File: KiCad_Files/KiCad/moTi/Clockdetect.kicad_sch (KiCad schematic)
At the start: 12 parts, among them Q1 NTK3139PT5G, U2 TLV3511DCKR, U5 SN74LVC1G3157DRLR

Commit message: HW file update
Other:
- title: MosaicTimeSync -> moTi
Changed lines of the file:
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@@
 	(paper "A3")
 	(title_block
-		(title "MosaicTimeSync")
+		(title "moTi")
 		(date "2025-09-02")
 		(rev "01")
@@
 		(comment 2 "Programme under the Fundamental Elements ")
 		(comment 3 "co-funded by the European Union Agency for the Space ")
-		(comment 4 "MosaicTimeSync project has been documented by Septentrio")
+		(comment 4 "moTi project has been documented by Septentrio")
 	)
 	(rectangle
@@
 				)
 				(justify right)
+				(hide yes)
 			)
 		)
@@
 				)
 				(justify left)
+				(hide yes)
 			)
 		)
@@
 				)
 				(justify left)
+				(hide yes)
 			)
 		)
@@
 				)
 				(justify left)
+				(hide yes)
 			)
 		)
@@
 				)
 				(justify right)
+				(hide yes)
 			)
 		)
@@
 				)
 				(justify right)
+				(hide yes)
 			)
 		)
@@
 		(dnp no)
 		(fields_autoplaced yes)
-		(property "Reference" "#PWR038"
+		(property "Reference" "#PWR?"
 			(at 114.3 45.72 0)
 			(effects
@@
 		(on_board yes)
 		(dnp no)
-		(property "Reference" "U2"
+		(property "Reference" "U?"
 			(at 298.196 174.244 0)
 			(effects
@@
 		(on_board yes)
 		(dnp no)
-		(property "Reference" "R11"
+		(property "Reference" "R?"
 			(at 267.97 180.848 90)
 			(effects
@@
 		(dnp no)
 		(fields_autoplaced yes)
-		(property "Reference" "C9"
+		(property "Reference" "C?"
 			(at 265.43 54.61 90)
 			(effects
@@
 		(on_board yes)
 		(dnp no)
-		(property "Reference" "R2"
+		(property "Reference" "R?"
 			(at 104.14 62.23 90)
 			(effects
@@
 		(dnp no)
 		(fields_autoplaced yes)
-		(property "Reference" "#PWR041"
+		(property "Reference" "#PWR?"
 			(at 288.29 195.58 0)
 			(effects
@@
 		(on_board yes)
 		(dnp no)
-		(property "Reference" "R10"
+		(property "Reference" "R?"
 			(at 252.73 175.768 90)
 			(effects
@@
 		(dnp no)
 		(fields_autoplaced yes)
-		(property "Reference" "#PWR047"
+		(property "Reference" "#PWR?"
 			(at 288.29 168.91 0)
 			(effects
@@
 		(on_board yes)
 		(dnp no)
-		(property "Reference" "R9"
+		(property "Reference" "R?"
 			(at 252.73 170.688 90)
 			(effects
@@
 		(on_board yes)
 		(dnp no)
-		(property "Reference" "C6"
+		(property "Reference" "C?"
 			(at 255.524 181.61 90)
 			(effects
@@
 		(dnp no)
 		(fields_autoplaced yes)
-		(property "Reference" "#PWR045"
+		(property "Reference" "#PWR?"
 			(at 105.41 224.79 0)
 			(effects
@@
 		(on_board yes)
 		(dnp no)
-		(property "Reference" "Q1"
+		(property "Reference" "Q?"
 			(at 87.63 214.63 90)
 			(effects
@@
 		(dnp no)
 		(fields_autoplaced yes)
-		(property "Reference" "R3"
+		(property "Reference" "R?"
 			(at 116.84 57.1499 0)
 			(effects
@@
 		(dnp no)
 		(fields_autoplaced yes)
-		(property "Reference" "#PWR042"
+		(property "Reference" "#PWR?"
 			(at 246.38 191.77 0)
 			(effects
@@
 		(dnp no)
 		(fields_autoplaced yes)
-		(property "Reference" "#PWR036"
+		(property "Reference" "#PWR?"
 			(at 82.55 132.08 0)
 			(effects
@@
 		(dnp no)
 		(fields_autoplaced yes)
-		(property "Reference" "U5"
+		(property "Reference" "U?"
 			(at 104.14 121.92 0)
 			(effects
@@
 		(dnp no)
 		(fields_autoplaced yes)
-		(property "Reference" "#PWR044"
+		(property "Reference" "#PWR?"
 			(at 69.85 224.79 0)
 			(effects
@@
 		(dnp no)
 		(fields_autoplaced yes)
-		(property "Reference" "#PWR048"
+		(property "Reference" "#PWR?"
 			(at 123.19 132.08 0)
 			(effects
@@
 		(dnp no)
 		(fields_autoplaced yes)
-		(property "Reference" "#PWR046"
+		(property "Reference" "#PWR?"
 			(at 246.38 175.26 0)
 			(effects
@@
 		(dnp no)
 		(fields_autoplaced yes)
-		(property "Reference" "C8"
+		(property "Reference" "C?"
 			(at 265.43 71.12 90)
 			(effects
@@
 		(dnp no)
 		(fields_autoplaced yes)
-		(property "Reference" "C7"
+		(property "Reference" "C?"
 			(at 88.9 57.15 90)
 			(effects

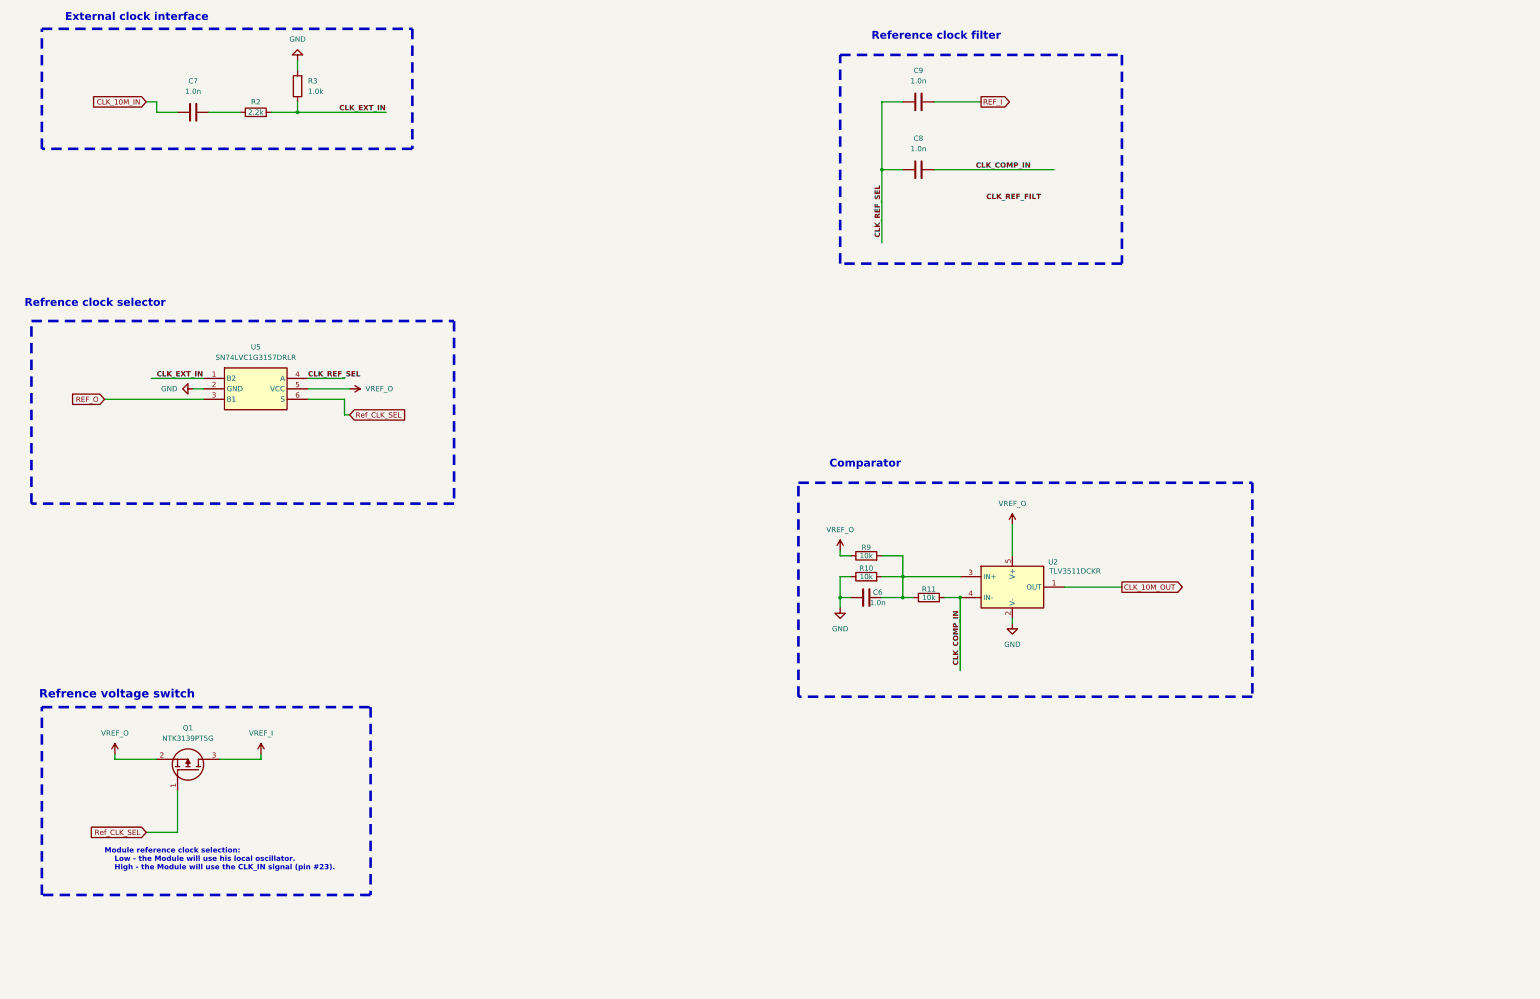
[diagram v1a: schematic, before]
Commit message: I2C change
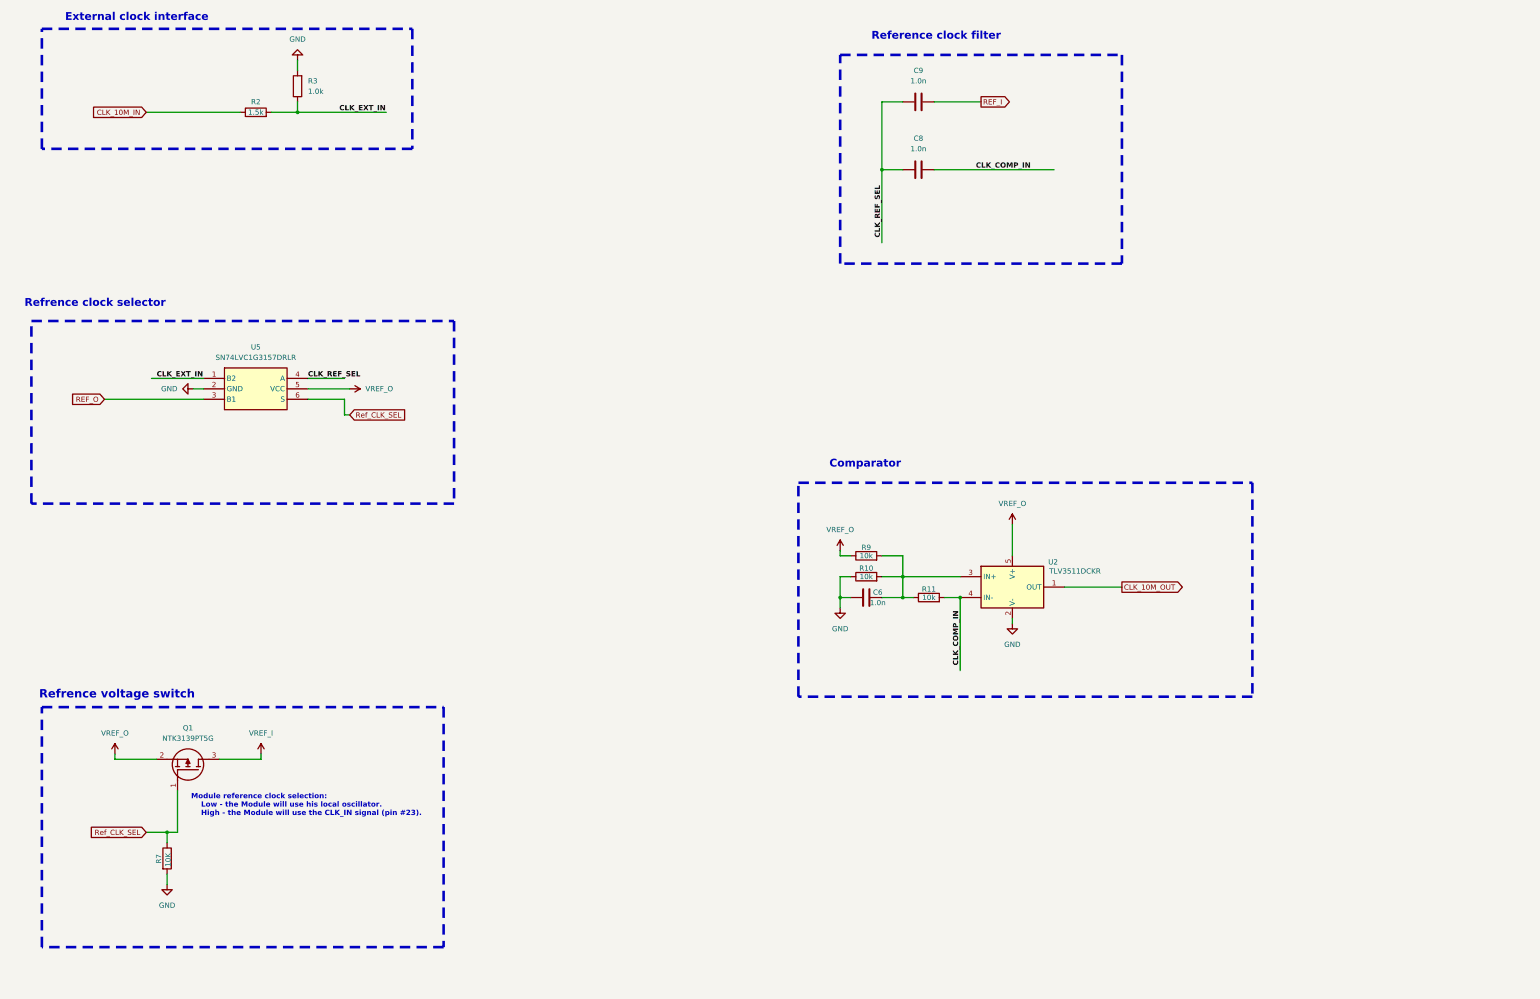
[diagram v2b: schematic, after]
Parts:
- removed C7: 1.0n, Capacitor_SMD:C_0402_1005Metric, symbol Device:C
- added R7: 10K, symbol Device:R
- R2: value 2.2k -> 1.5k
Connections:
- net CLK_10M_IN: now also R2.1
- net GND: now also R7.2
- net Ref_CLK_SEL: now also R7.1

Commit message: BOM update
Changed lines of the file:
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@@
 		(in_pos_files yes)
 		(dnp no)
-		(fields_autoplaced yes)
 		(property "Reference" "R3"
-			(at 116.84 57.1499 0)
+			(at 116.078 58.42 0)
 			(show_name no)
 			(do_not_autoplace no)
@@
 		)
 		(property "Value" "1.0k"
-			(at 116.84 59.6899 0)
+			(at 114.3 60.452 90)
 			(show_name no)
 			(do_not_autoplace no)

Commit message: general clean up
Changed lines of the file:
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@@
 		(title "moTi")
 		(date "2025-09-02")
-		(rev "01")
+		(rev "02")
 		(company "Septentrio")
 		(comment 1 "Grant EUSPA/GRANT/02/2024")
@@
 		(comment 3 "co-funded by the European Union Agency for the Space ")
 		(comment 4 "moTi project has been documented by Septentrio")
+		(comment 5 "  ")
 	)
 	(rectangle
@@
 		)
 	)
+	(text_box "Schematics arranged by Laetitia.K"
+		(exclude_from_sim no)
+		(at 373.38 275.59 0)
+		(size 35.56 3.9483)
+		(margins 0.9525 0.9525 0.9525 0.9525)
+		(stroke
+			(width -0.0001)
+			(type solid)
+		)
+		(fill
+			(type none)
+		)
+		(effects
+			(font
+				(size 1.27 1.27)
+				(color 132 0 0 1)
+			)
+			(justify left top)
+		)
+	)
 	(junction
 		(at 82.55 240.03)
@@
 			(project "Clockdetect"
 				(path "/d367677d-48cb-42d1-9e76-ef4b69e236f6"
-					(reference "U?")
+					(reference "U2")
 					(unit 1)
 				)
@@
 			(project "Clockdetect"
 				(path "/d367677d-48cb-42d1-9e76-ef4b69e236f6"
-					(reference "C?")
+					(reference "C9")
 					(unit 1)
 				)
@@
 			(project "Clockdetect"
 				(path "/d367677d-48cb-42d1-9e76-ef4b69e236f6"
-					(reference "R?")
+					(reference "R2")
 					(unit 1)
 				)
@@
 				)
 			)
+			(project "Clockdetect"
+				(path "/d367677d-48cb-42d1-9e76-ef4b69e236f6"
+					(reference "R14")
+					(unit 1)
+				)
+			)
 		)
 	)
@@
 			(project "Clockdetect"
 				(path "/d367677d-48cb-42d1-9e76-ef4b69e236f6"
-					(reference "Q?")
+					(reference "Q1")
 					(unit 1)
 				)
@@
 			(project "Clockdetect"
 				(path "/d367677d-48cb-42d1-9e76-ef4b69e236f6"
-					(reference "R?")
+					(reference "R3")
 					(unit 1)
 				)
@@
 				)
 			)
+			(project "Clockdetect"
+				(path "/d367677d-48cb-42d1-9e76-ef4b69e236f6"
+					(reference "#PWR07")
+					(unit 1)
+				)
+			)
 		)
 	)
@@
 			(project "Clockdetect"
 				(path "/d367677d-48cb-42d1-9e76-ef4b69e236f6"
-					(reference "U?")
+					(reference "U5")
 					(unit 1)
 				)
@@
 			(project "Clockdetect"
 				(path "/d367677d-48cb-42d1-9e76-ef4b69e236f6"
-					(reference "C?")
+					(reference "C8")
 					(unit 1)
 				)
